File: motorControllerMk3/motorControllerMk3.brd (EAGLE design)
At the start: 54.6 x 49.8 mm, 41 parts, among them J1 AVR_SPI_PRG_6NS

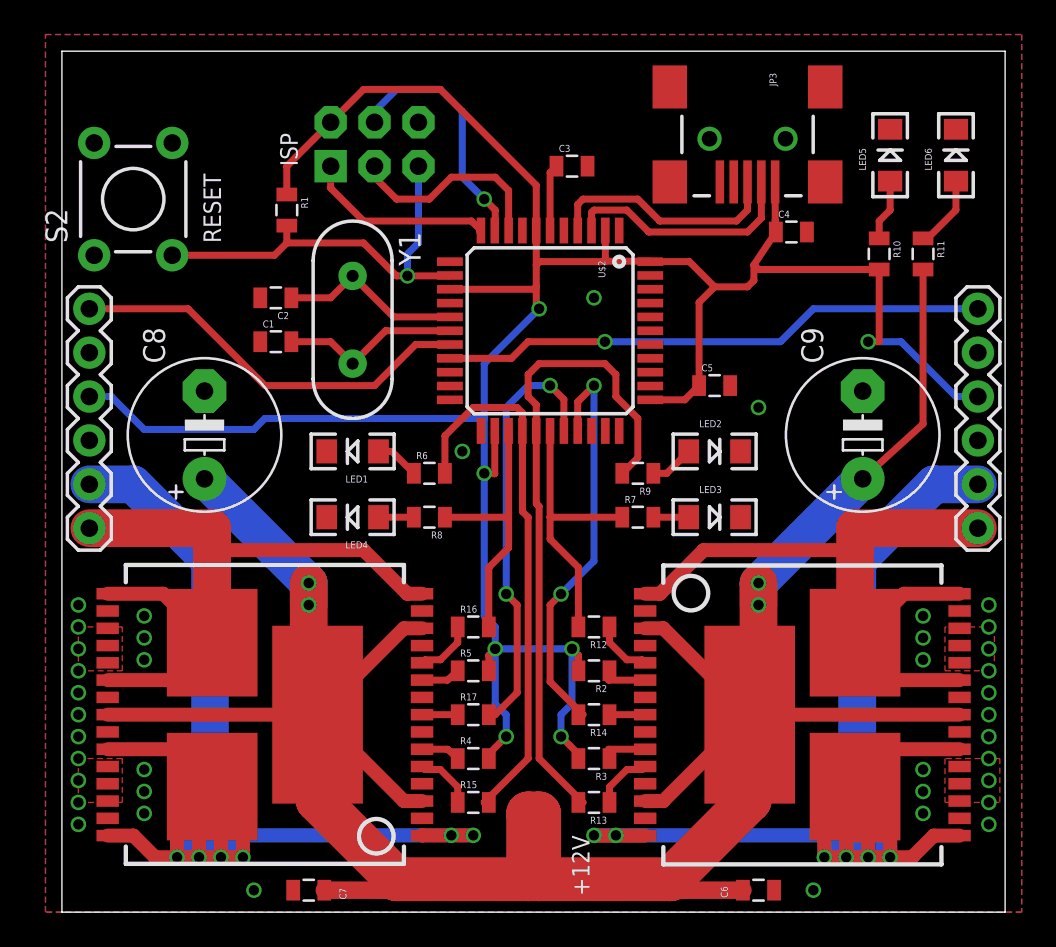
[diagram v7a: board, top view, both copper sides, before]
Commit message: fixed mistakes in layout, added usb resistors
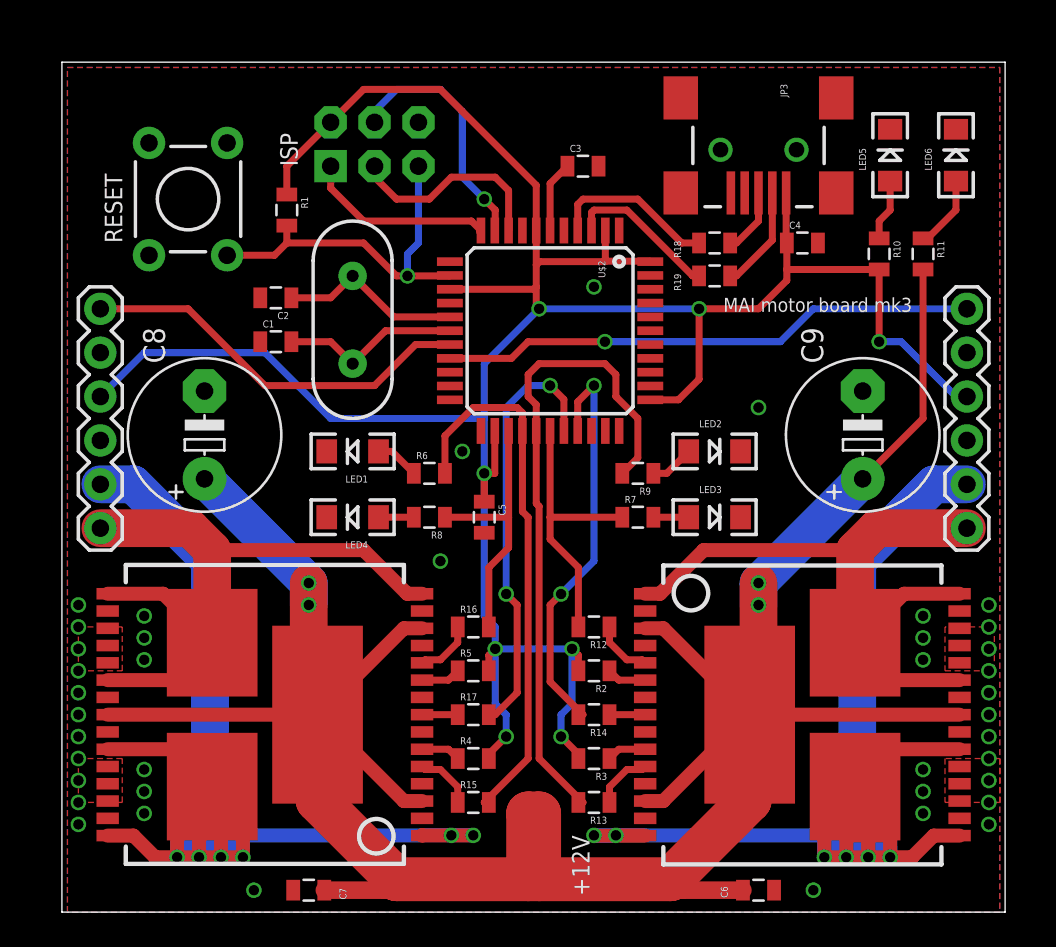
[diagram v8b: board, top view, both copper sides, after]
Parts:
- added R18, R19: 22R, SparkFun-Passives:0805
- C3: value 1n -> 1u
- JP1: value (none) -> m1
- JP2: value (none) -> m2
- Y1: value (none) -> 16MHz
- moved C5 15.4 mm to (47.6, 33.0), turned to 270 degrees
- moved S2 3.18 mm to (30.5, 51.4)
- moved C4 0.90 mm to (66.0, 48.9)
- moved JP3 0.90 mm to (63.5, 54.3)
- moved C3 0.64 mm to (53.3, 53.3)
- moved JP1 0.64 mm to (75.6, 32.4)
- moved JP2 0.63 mm to (25.4, 32.4)
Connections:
- new net N$14: JP3.D+, R18.1
- new net N$15: JP3.D-, R19.1
- net N$10: now also R18.2; no longer JP3.D+
- net N$11: now also R19.2; no longer JP3.D-
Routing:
- net N$15: track 0.00 -> 6.03 mm
- net N$11: track 13.9 -> 8.91 mm
- net N$10: track 13.9 -> 9.72 mm
- net +5V: track 152.5 -> 156.6 mm, vias 7 -> 8
- net N$14: track 0.00 -> 3.79 mm
- net N$38: track 24.8 -> 21.6 mm
- net OUTA1: track 41.1 -> 39.7 mm
- net OUTB2: track 41.1 -> 39.7 mm
- net OUTB1: track 85.0 -> 84.4 mm
- net PD1: track 31.8 -> 31.1 mm
- net PD0: track 23.7 -> 23.1 mm
- net OUTA2: track 86.6 -> 86.0 mm
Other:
- board size 54.6 x 49.8 mm -> 54.6 x 49.2 mm
- board text added: "MAI motor board mk3"
